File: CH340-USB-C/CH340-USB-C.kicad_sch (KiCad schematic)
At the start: 15 parts

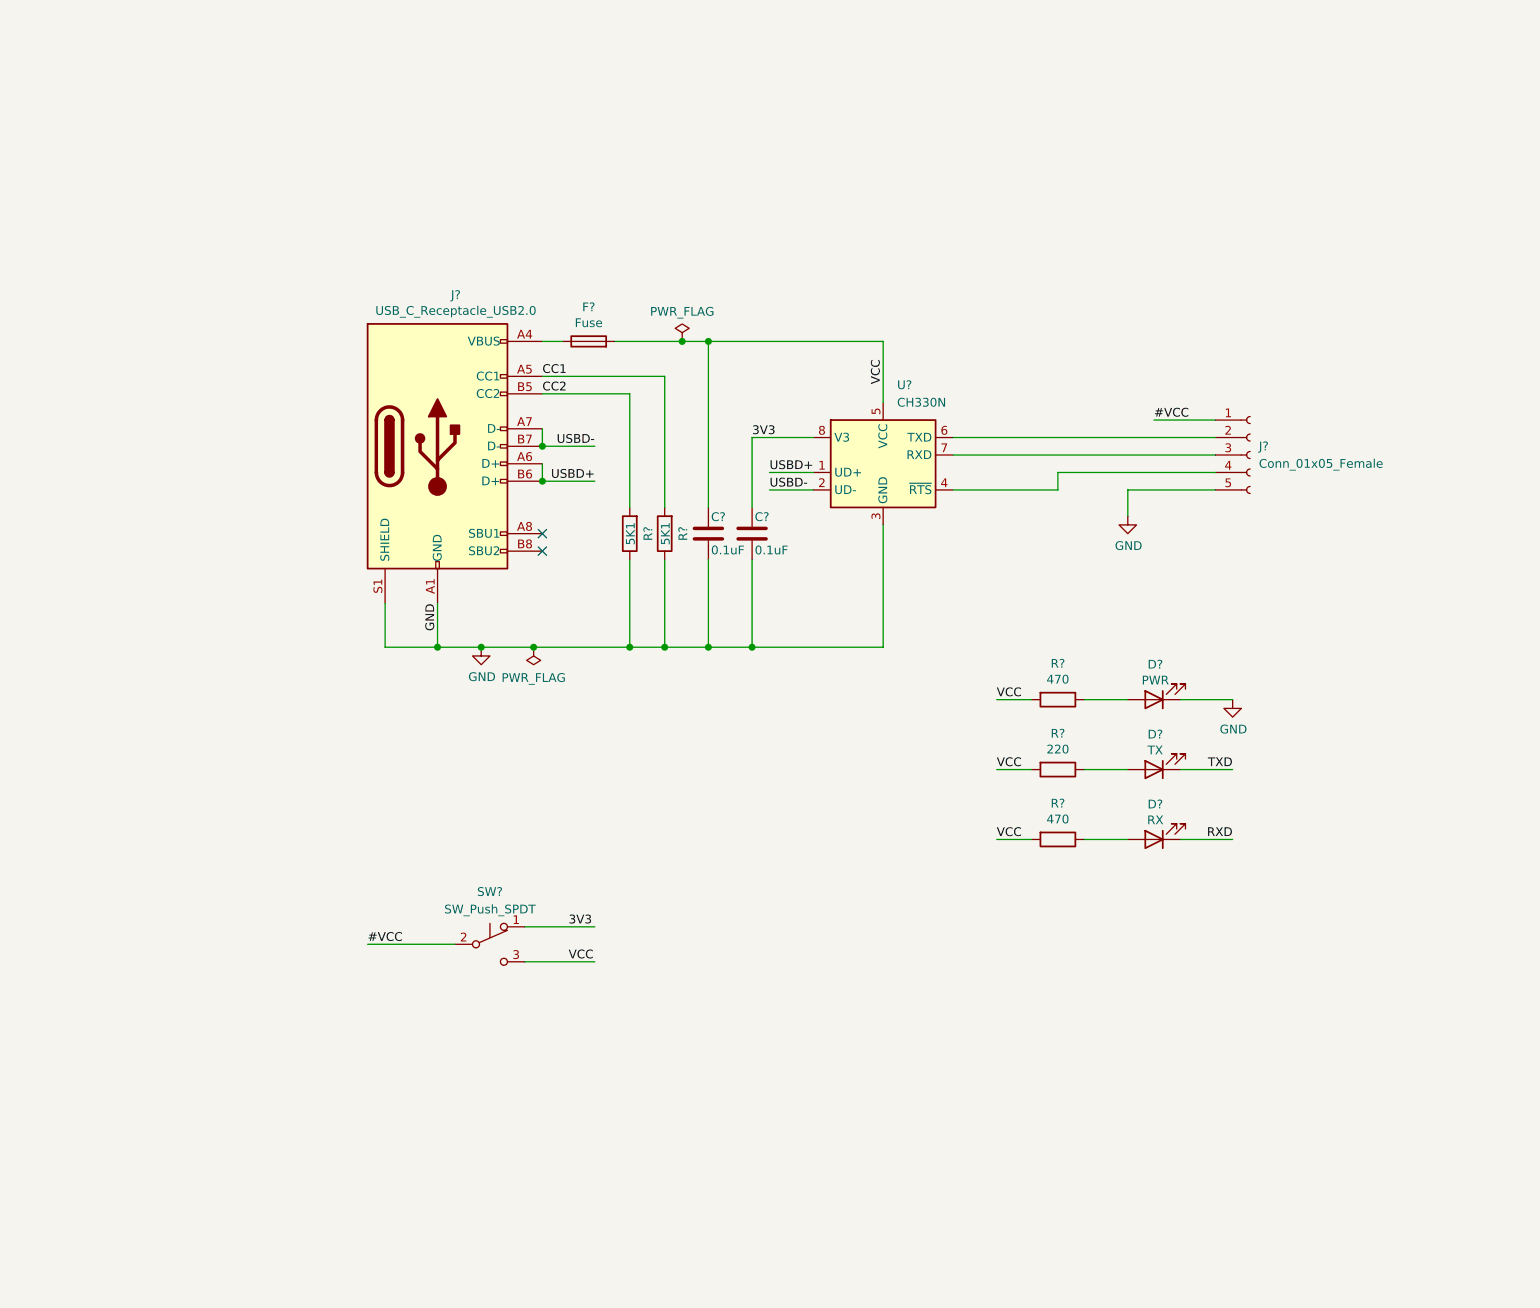
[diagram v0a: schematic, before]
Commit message: add LDO
Linear Voltage Regulators XC6206
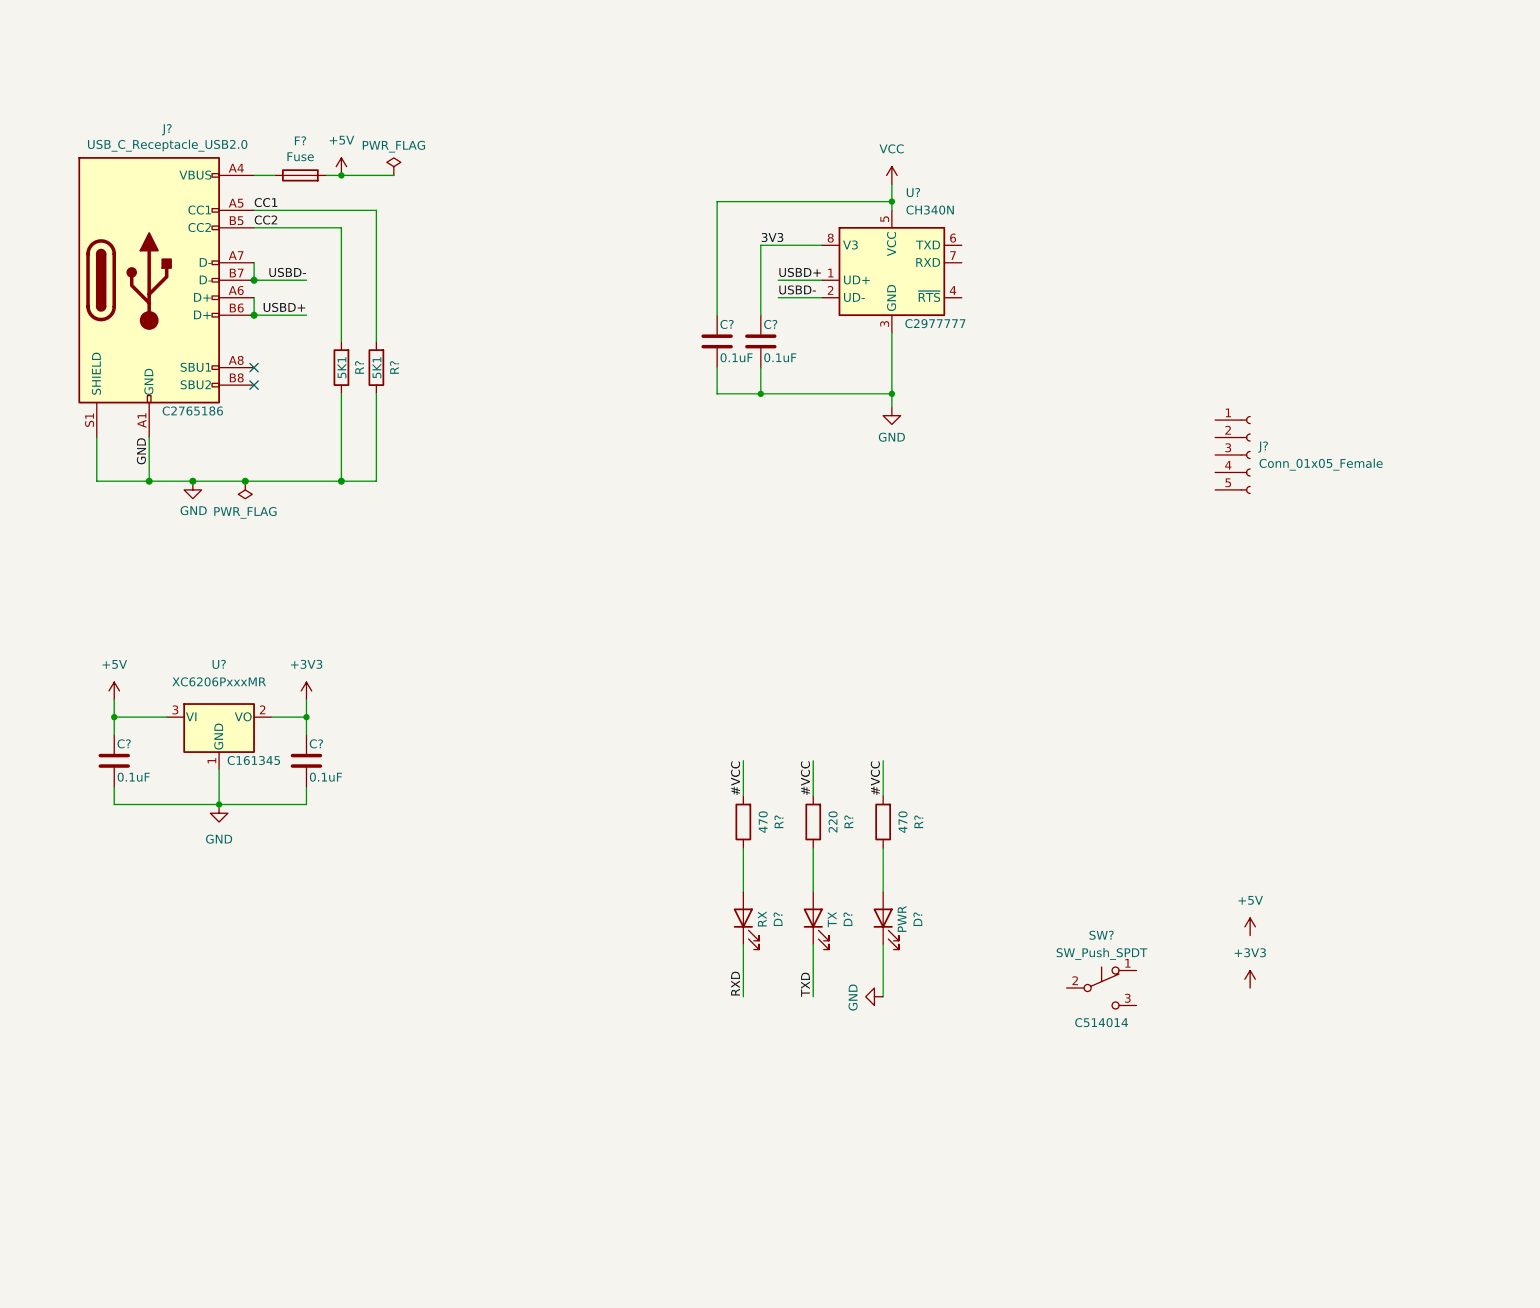
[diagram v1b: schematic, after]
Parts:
- added C? (x2): 0.1uF, Capacitor_SMD:C_0805_2012Metric, symbol Device:C
- added U?: XC6206PxxxMR, Package_TO_SOT_SMD:SOT-23, symbol Regulator_Linear:XC6206PxxxMR
- J?: LCSC (none) -> C2765186
- SW?: footprint Button_Switch_THT:SW_PUSH_E-Switch_FS5700DP_DPDT -> Button_Switch_SMD:SW_SPDT_PCM12; LCSC (none) -> C514014
- U?: value CH330N -> CH340N; LCSC (none) -> C2977777
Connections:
- net #VCC: now also R?.2, R?.2, R?.2; no longer J?.1 (Pin_1), SW?.2 (B)
- net 3V3: no longer SW?.1 (A)
- net GND: now also C?.2, C?.2, U?.1 (GND); no longer J?.5 (Pin_5)
- net VCC: no longer F?.2, R?.2, R?.2, R?.2, SW?.3 (C)
- net at J?.2 (Pin_2): no longer U?.6 (TXD)
- net at J?.3 (Pin_3): no longer U?.7 (RXD)
- net at J?.4 (Pin_4): no longer U?.4 (~{RTS})
- new net +3V3: C?.1, U?.2 (VO)
- new net +5V: C?.1, F?.2, U?.3 (VI)
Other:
- moved on the sheet: C?, D?, F?, J?, R?, SW?, U?

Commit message: add Device
add 3v3 Led & SPDT Switch Voltage
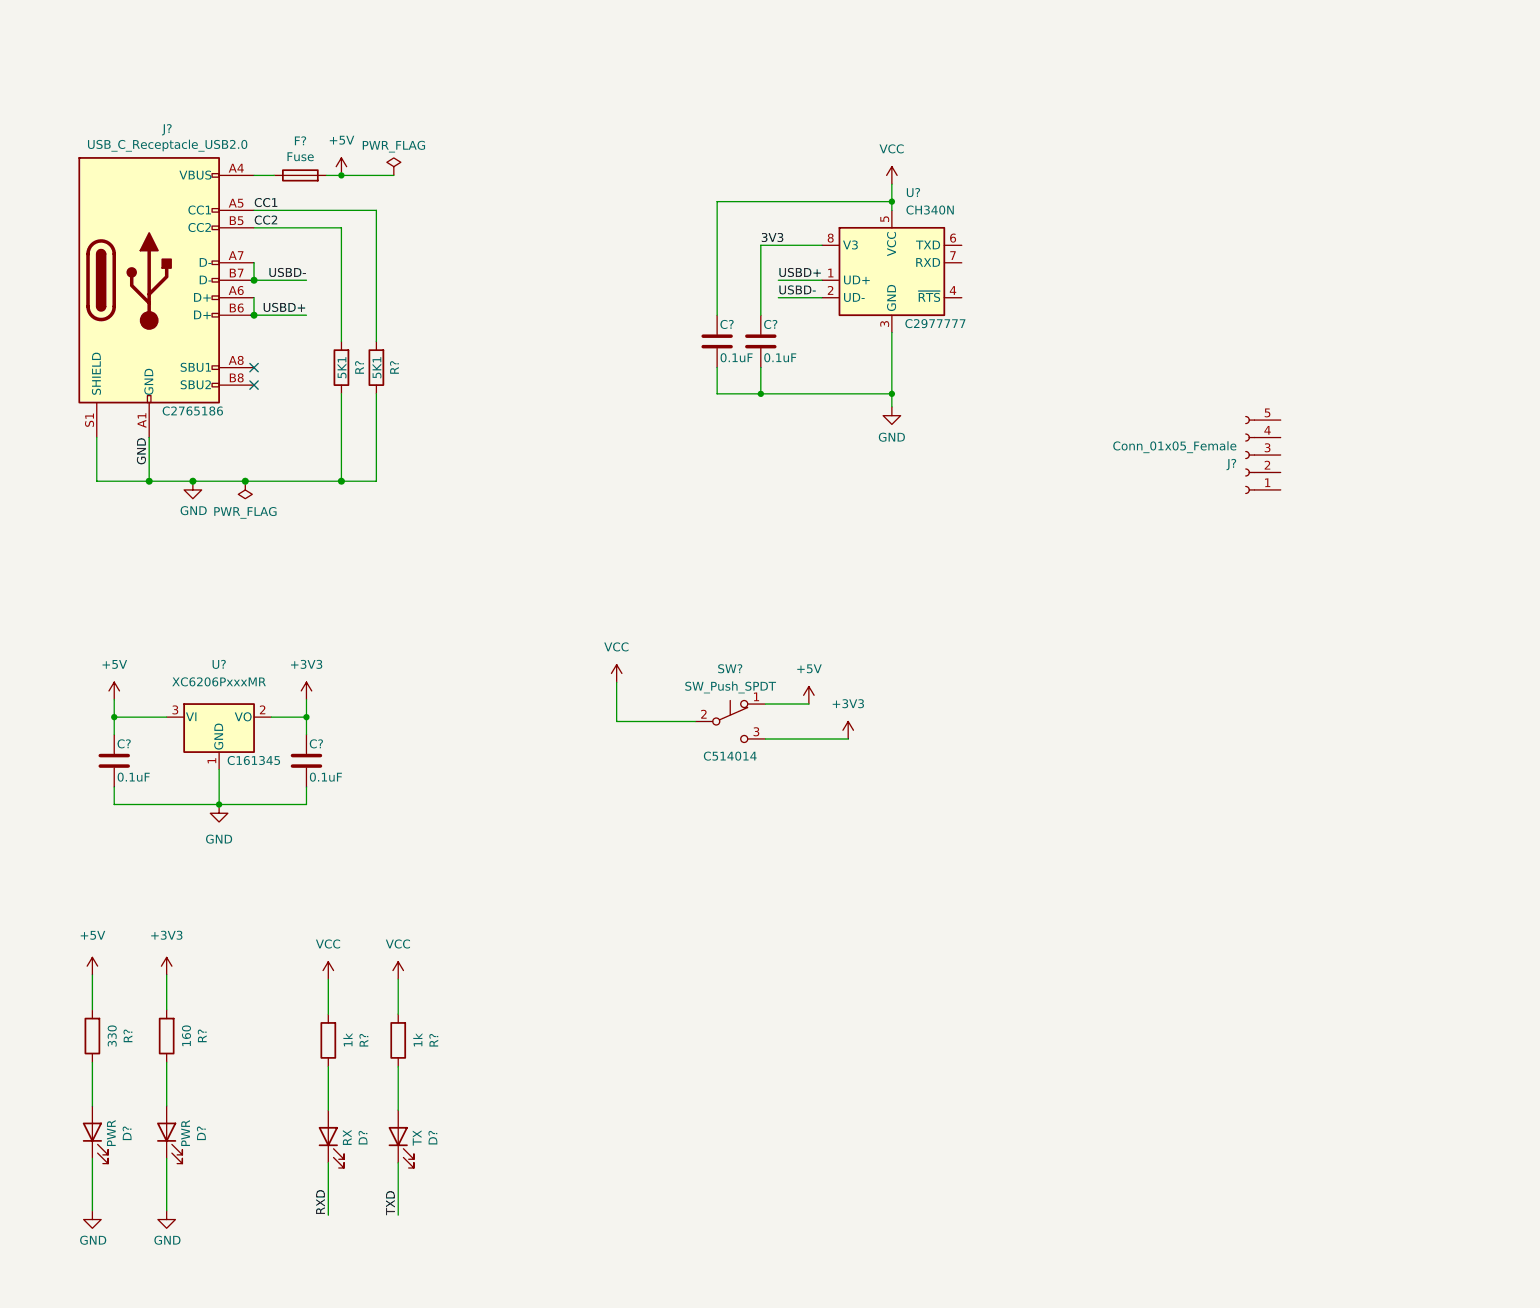
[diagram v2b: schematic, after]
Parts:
- added D?: PWR, LED_SMD:LED_0805_2012Metric, symbol Device:LED
- added R?: 160, Resistor_SMD:R_0805_2012Metric, symbol Device:R
- R?: value 220 -> 1k
- R?: value 470 -> 330
- R?: value 470 -> 1k
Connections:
- net +3V3: now also SW?.3 (C), R?.2
- net +5V: now also R?.2, SW?.1 (A)
- net GND: now also D?.1 (K)
- net VCC: now also R?.2, R?.2, SW?.2 (B)
- removed net #VCC: R?.2, R?.2, R?.2
- new net: D?.2 (A), R?.1
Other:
- moved on the sheet: D?, J?, R?, SW?

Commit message: remove Pwr LED
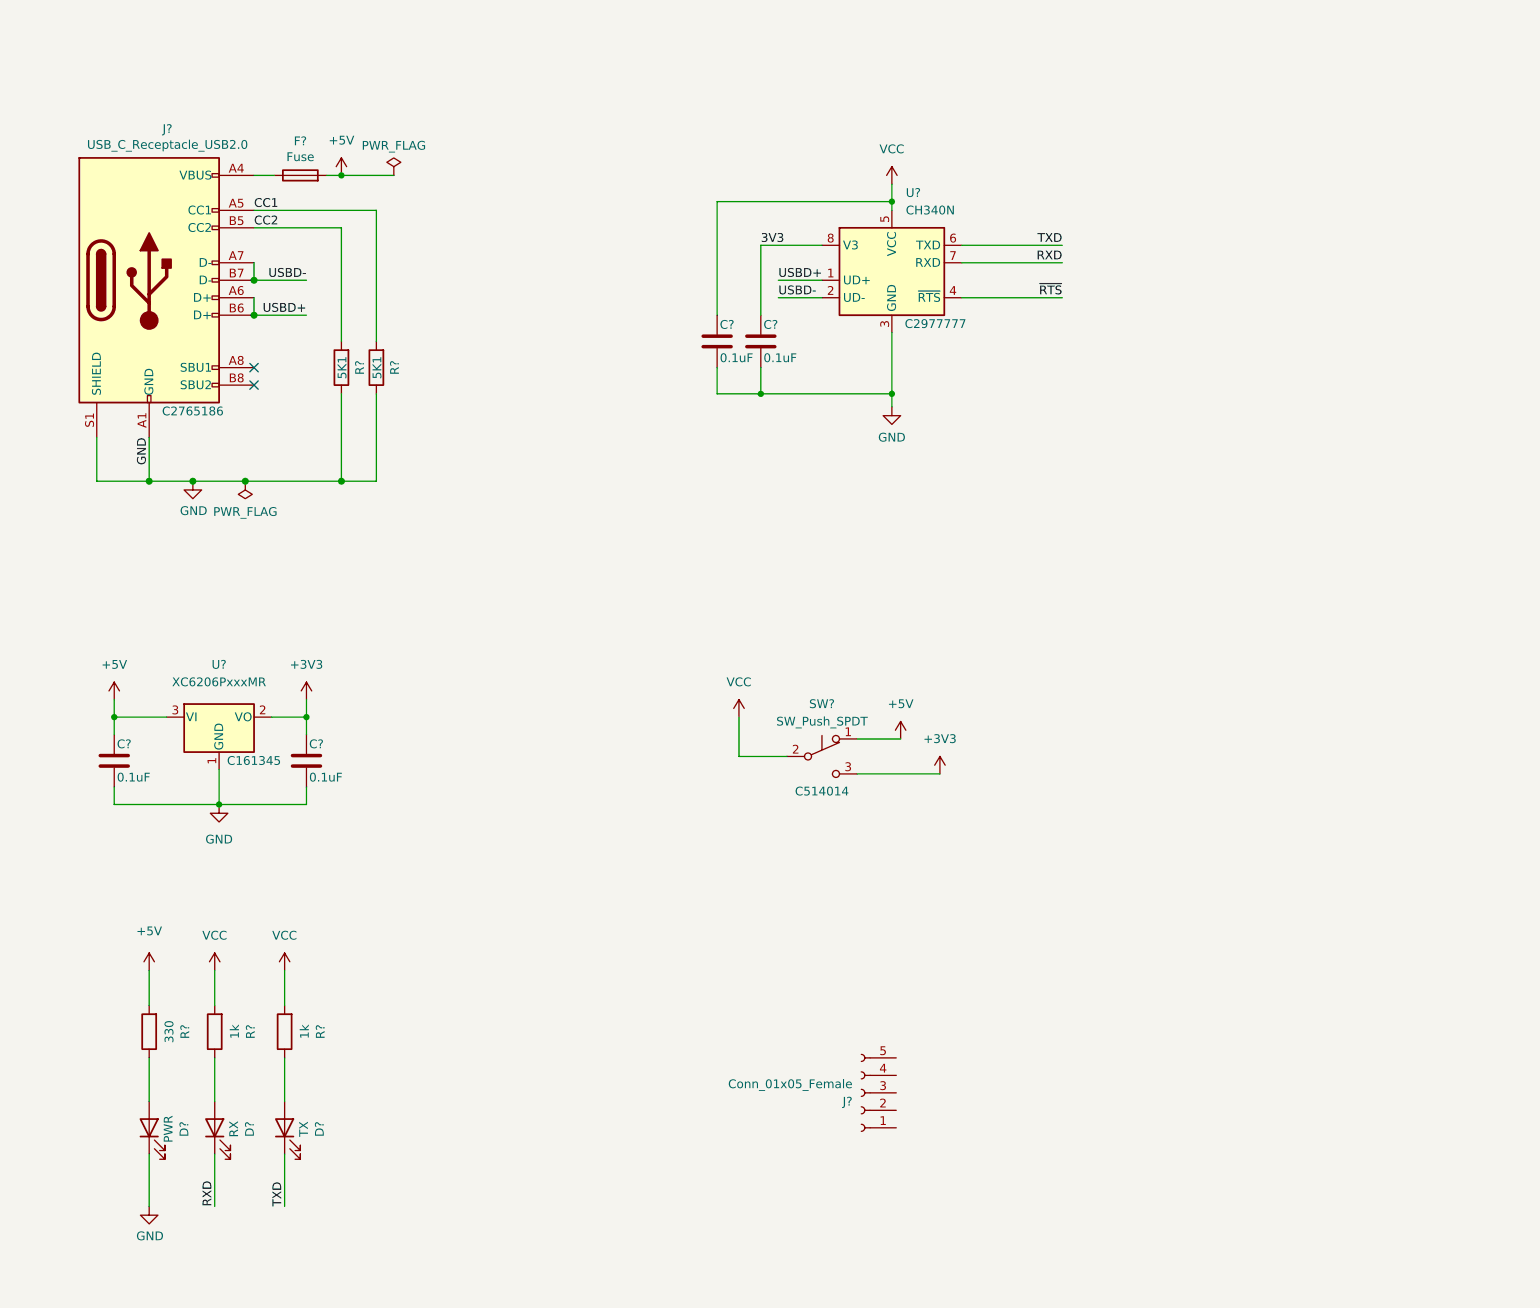
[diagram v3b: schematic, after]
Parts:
- removed D?: PWR, LED_SMD:LED_0805_2012Metric, symbol Device:LED
- removed R?: 160, Resistor_SMD:R_0805_2012Metric, symbol Device:R
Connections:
- net RXD: now also U?.7 (RXD)
- net TXD: now also U?.6 (TXD)
- net ~{RTS}: now reaches U?.4 (~{RTS})
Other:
- moved on the sheet: D?, J?, R?, SW?

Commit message: 調整
調整版面
新增保險絲LCSC 編號
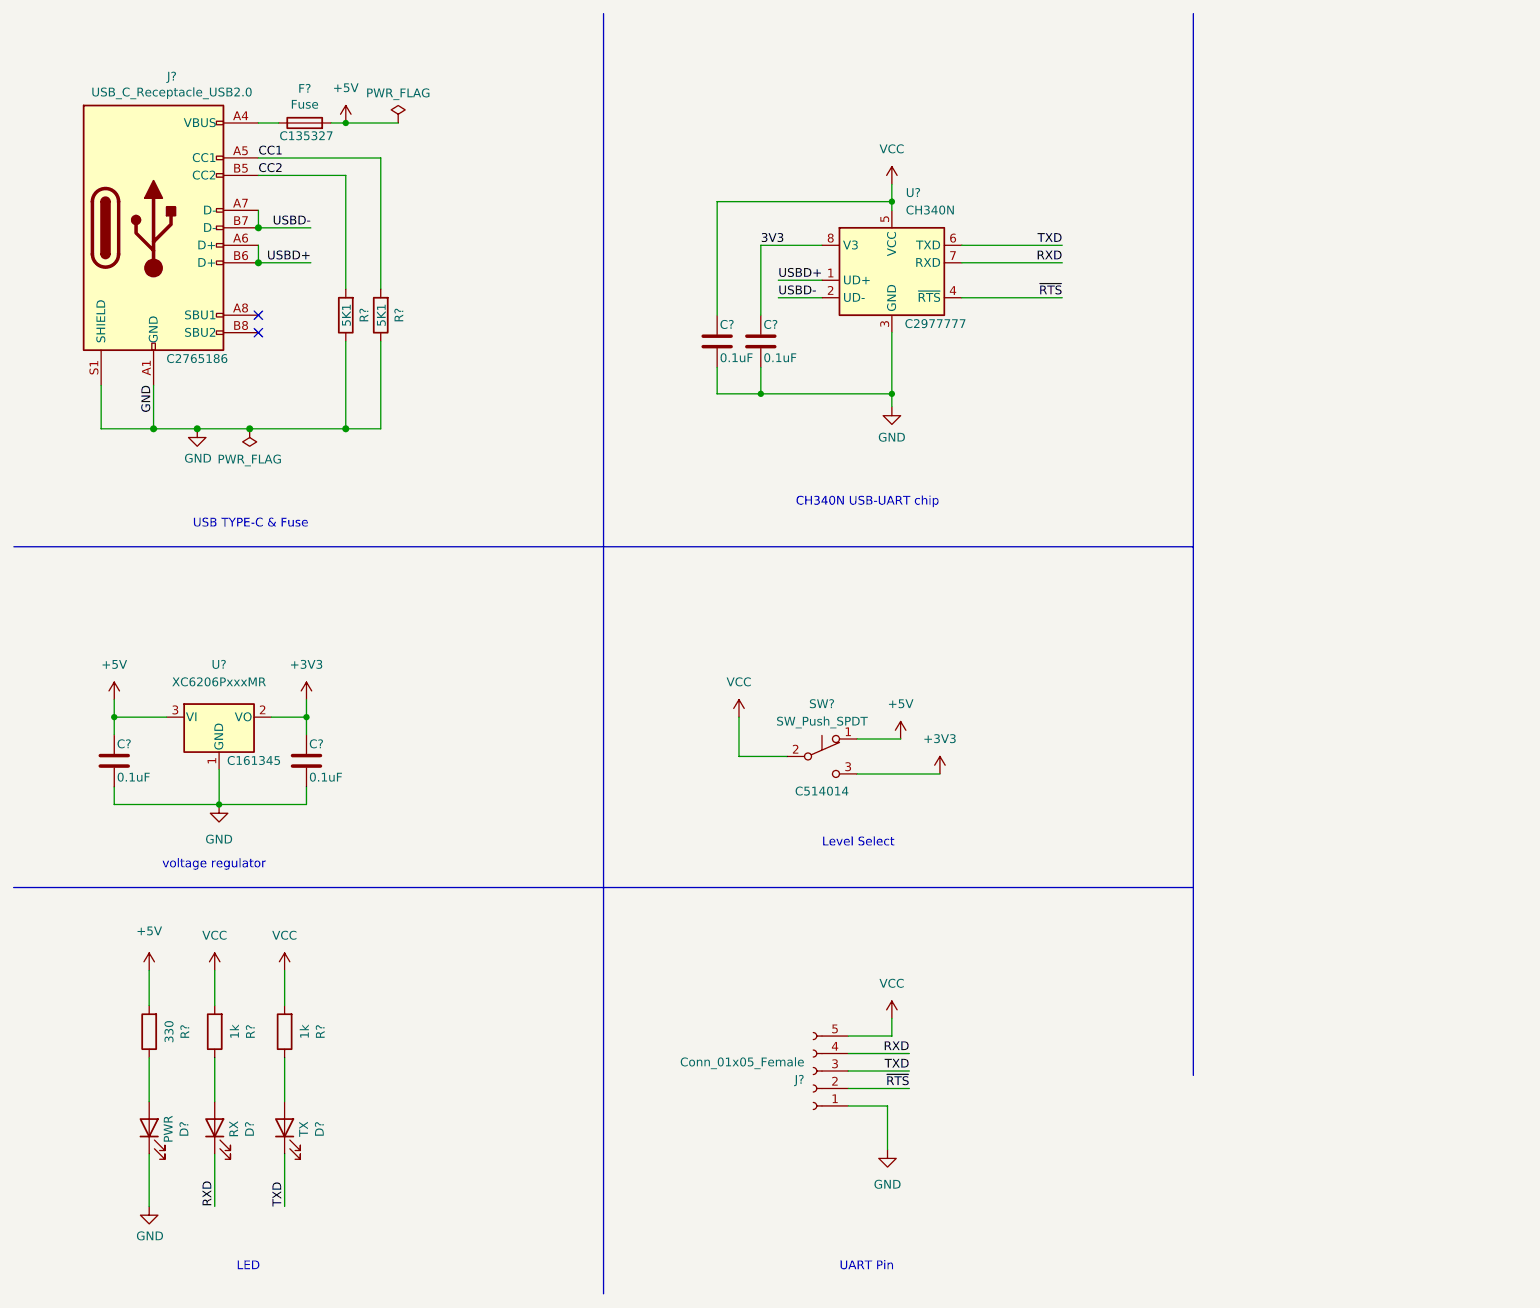
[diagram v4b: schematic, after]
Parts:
- F?: LCSC (none) -> C135327
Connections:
- net GND: now also J?.1 (Pin_1)
- net RXD: now also J?.4 (Pin_4)
- net TXD: now also J?.3 (Pin_3)
- net VCC: now also J?.5 (Pin_5)
- net ~{RTS}: now also J?.2 (Pin_2)
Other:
- note added: "CH340N USB-UART chip"
- note added: "LED"
- note added: "Level Select"
- note added: "UART Pin"
- note added: "USB TYPE-C & Fuse"
- note added: "voltage regulator"
- moved on the sheet: F?, J?, R?
